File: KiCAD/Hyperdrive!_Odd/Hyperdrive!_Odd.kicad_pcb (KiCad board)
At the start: 2 copper layers, 103.9 x 73.1 mm, 63 parts, among them K1 ES1, K2 ES2, K3 ES3, K4 ES4, P1 H-Bridge PCB, P2 H-Bridge PCB, P3 Main Processor PCB, P4 MR, P5 ML, P7 RIR PCB, U1 MAX14780, U10 TSOP4038, U2 QRE1113, U3 QRE1113, U4 MAX14780, U5 QRE1113, U6 QRE1113, U7 MCP6541, U8 QRE1113, U9 QRE1113

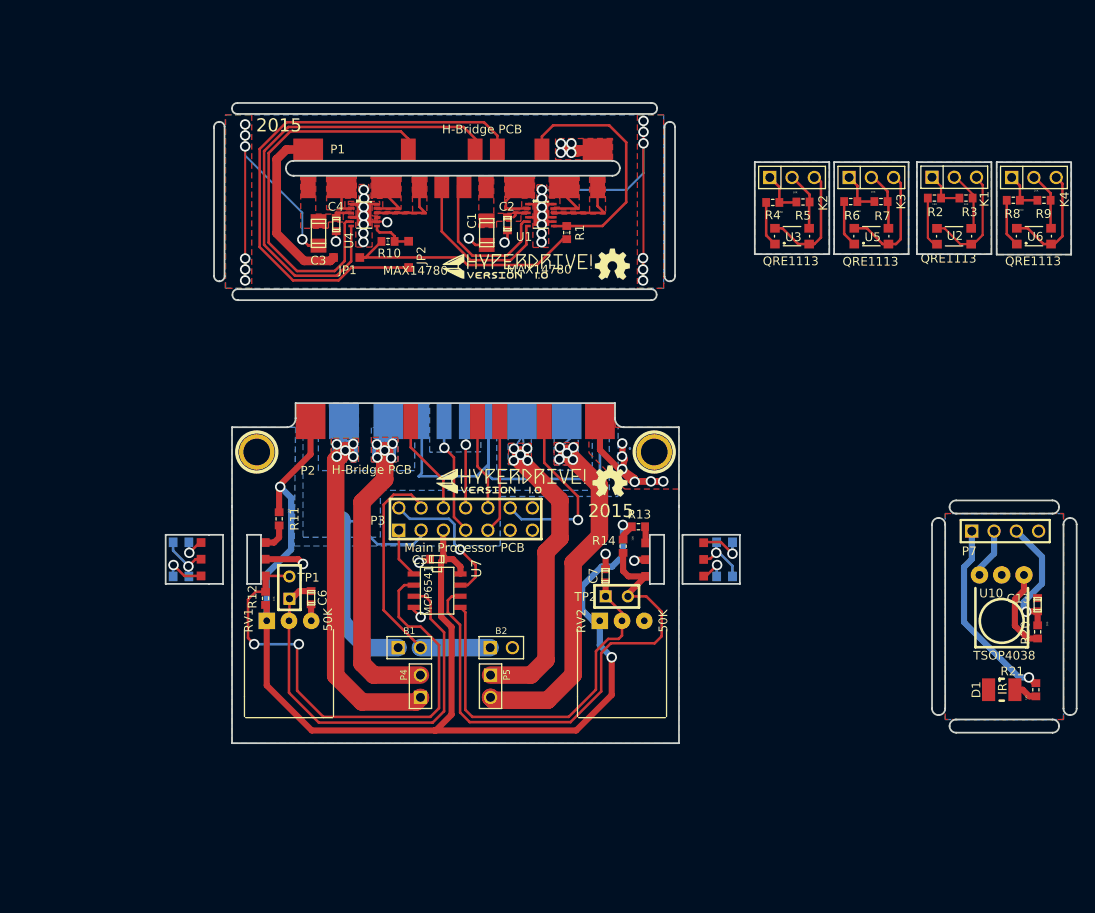
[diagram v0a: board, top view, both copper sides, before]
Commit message: Updated 3D-Model, and PCBs.
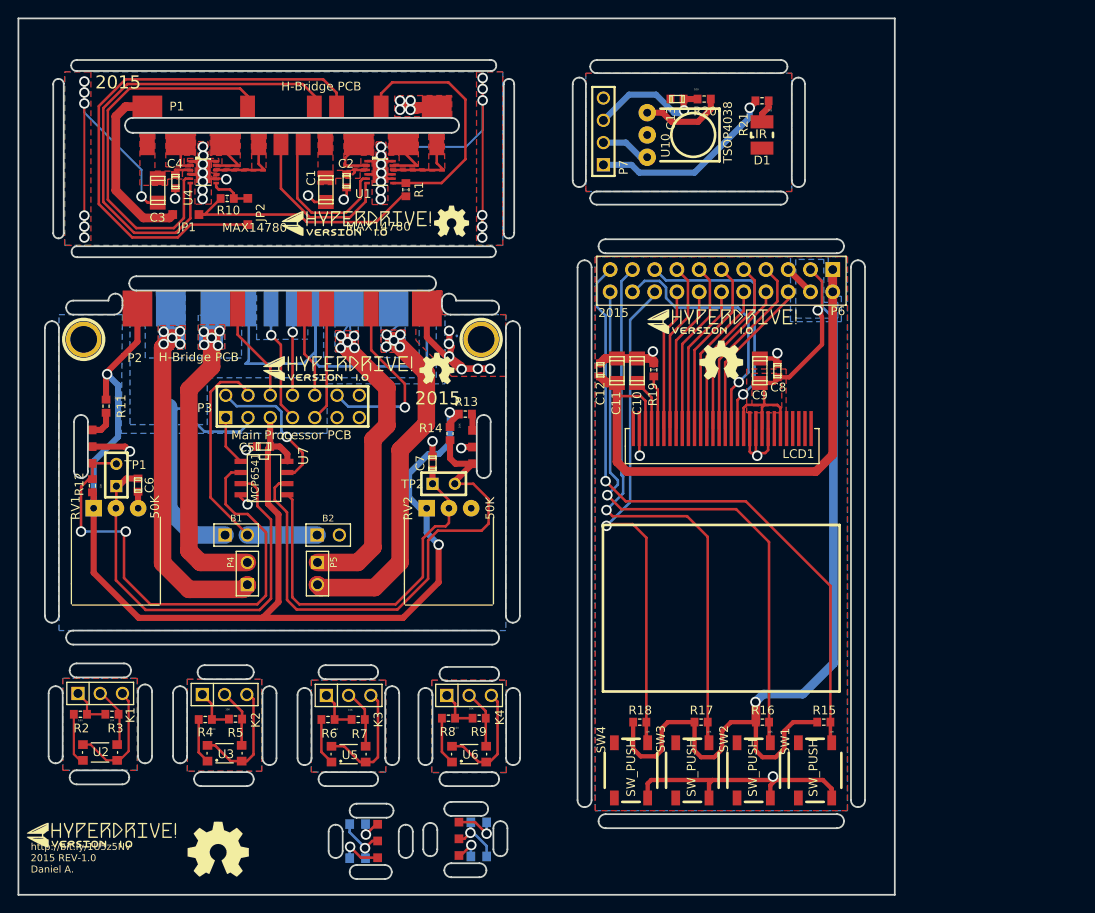
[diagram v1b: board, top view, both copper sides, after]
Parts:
- added ?: , OSHW-logo_silkscreen-front_5mm, F.Cu at (234.2, 117.0)
- added ?: , Hyperdrive!_F.SilkS_20mm, F.Cu at (234.2, 112.6)
- added C10: 4.7u, c_1206, F.Cu at (224.6, 118.2)
- added C11: 2.2u, c_1206, F.Cu at (222.3, 118.2)
- added C12: 100n, c_0603, F.Cu at (220.4, 118.1)
- added C8: 100n, c_0603, F.Cu at (240.6, 118.2)
- added C9: 2.2u, c_1206, F.Cu at (238.6, 118.2)
- added G***: OSHW-logo_silkscreen-back_7mm, OSHW-logo_silkscreen-back_7mm, F.Cu at (176.8, 172.8)
- added LCD1: 128X64_LCD, DP, F.Cu at (234.7, 124.8)
- added P6: , CON_11x2, F.Cu at (239.3, 109.2)
- added R15: 10K, r_0603, F.Cu at (245.9, 158.3)
- added R16: 10K, r_0603, F.Cu at (238.9, 158.3)
- added R17: 10K, r_0603, F.Cu at (231.9, 158.3)
- added R18: 10K, r_0603, F.Cu at (224.9, 158.3)
- added R19: 560K, r_0603, F.Cu at (226.5, 118.1)
- added SW1: SW_PUSH, TL3342, F.Cu at (244.9, 163.8)
- added SW2: SW_PUSH, TL3342, F.Cu at (237.9, 163.8)
- added SW3: SW_PUSH, TL3342, F.Cu at (230.9, 163.8)
- added SW4: SW_PUSH, TL3342, F.Cu at (223.9, 163.8)
- added VAL: REF, Hyperdrive!_F.SilkS_20mm, F.Cu at (163.4, 171.2)
- U2, U3, U5, U6: value QRE1113 -> (none)
- moved K1 113.9 mm to (163.3, 155.0)
- moved R2 113.9 mm to (161.1, 157.4)
- moved R3 113.9 mm to (164.7, 157.4)
- moved U2 113.9 mm to (163.3, 161.8)
- moved K2 87.6 mm to (177.5, 155.2)
- moved R4 87.6 mm to (175.3, 158.0)
- moved U3 87.6 mm to (177.5, 161.8)
- moved R5 87.6 mm to (178.8, 157.9)
- moved K4 87.4 mm to (205.4, 155.2)
- moved R8 87.4 mm to (203.1, 157.8)
- moved R9 87.4 mm to (206.6, 157.8)
- moved U6 87.4 mm to (205.4, 161.9)
- moved R6 84.0 mm to (189.3, 158.0)
- moved R7 84.0 mm to (192.8, 158.0)
- moved K3 84.0 mm to (191.7, 155.2)
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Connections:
- ? pad 1: N-000009 -> N-0000011 (x2)
- ? pad 3: N-0000044 -> N-0000010 (x2)
- ? pad 1: N-0000013 (its old number) -> N-000005 (x2)
- ? pad 3: N-0000012 (its old number) -> N-000004 (x2)
- C7 pad 1: N-0000062 -> N-0000039
- R11 pad 2: N-0000045 -> N-0000010
- R12 pad 2: N-0000014 (its old number) -> N-0000011
- R13 pad 2: N-0000016 (its old number) -> N-000004
- R14 pad 2: N-0000017 -> N-000005
- RV2 pad 2: N-0000062 -> N-0000039
- TP1 pad 2: N-000009 -> N-0000011
- TP2 pad 1: N-0000050 -> N-0000039
- TP2 pad 2: N-0000013 (its old number) -> N-000005
- U7 pad 2: N-0000014 (its old number) -> N-0000011
- U7 pad 5: N-0000062 -> N-0000039
- U7 pad 6: N-0000017 -> N-000005
- U8 pad 1: N-0000045 -> N-0000010
- U8 pad 3: N-0000014 (its old number) -> N-0000011
- U9 pad 1: N-0000016 (its old number) -> N-000004
- U9 pad 3: N-0000017 -> N-000005
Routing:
- net +3.3VB: track 0.00 -> 142.9 mm, vias 0 -> 2
- net /ST1: track 0.00 -> 73.7 mm, vias 0 -> 1
- net /ST2: track 0.00 -> 67.7 mm, vias 0 -> 1
- net VCC: track 0.00 -> 66.0 mm
- net /ST3: track 0.00 -> 65.2 mm, vias 0 -> 1
- net N-000005: track 0.00 -> 63.8 mm, vias 0 -> 1
- net N-0000011: track 0.00 -> 62.8 mm, vias 0 -> 3
- net GNDB: track 0.00 -> 59.0 mm, vias 0 -> 5
- net /ST4: track 0.00 -> 57.7 mm, vias 0 -> 1
- net N-0000014 (its old number): track 57.3 -> 0.00 mm, vias 3 -> 0
- net N-0000039: track 0.00 -> 43.4 mm
- net N-0000017: track 42.3 -> 0.00 mm
- net N-0000062: track 40.7 -> 0.00 mm
- net /RES#: track 0.00 -> 29.6 mm, vias 0 -> 1
- net /CS#: track 0.00 -> 29.4 mm, vias 0 -> 1
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- added copper zone on B.Cu, net +3.3VB
- added copper zone on F.Cu, net +3.3VB
- added copper zone on B.Cu, net GNDB
- added copper zone on F.Cu, net GNDB
- added copper zone on B.Cu, net N-0000015
- added copper zone on F.Cu, net N-0000015
- added copper zone on B.Cu, net N-0000023
- added copper zone on F.Cu, net N-0000023
- added copper zone on B.Cu, net N-0000024
- added copper zone on F.Cu, net N-0000024
- added copper zone on B.Cu, net N-0000032
- added copper zone on F.Cu, net N-0000032
- removed copper zone on F.Cu, net (none)
- removed copper zone on B.Cu, net N-0000031 (its old number)
- removed copper zone on F.Cu, net N-0000031 (its old number)
- removed copper zone on B.Cu, net N-0000035 (its old number)
- removed copper zone on F.Cu, net N-0000035 (its old number)
- removed copper zone on B.Cu, net N-0000037
- removed copper zone on F.Cu, net N-0000037
- removed copper zone on B.Cu, net N-0000043
- removed copper zone on F.Cu, net N-0000043
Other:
- board size 103.9 x 73.1 mm -> 100 x 100 mm
- board text added: "http://bit.ly/1U5z5Nv 2015 REV-1.0 Daniel A."
